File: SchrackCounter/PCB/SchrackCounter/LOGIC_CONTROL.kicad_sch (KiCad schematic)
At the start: 7 parts, among them U1 LTD080BUE-103A, U2 LTD080BUE-103A, U3 LTD080BUE-103A, U6 MAX7219

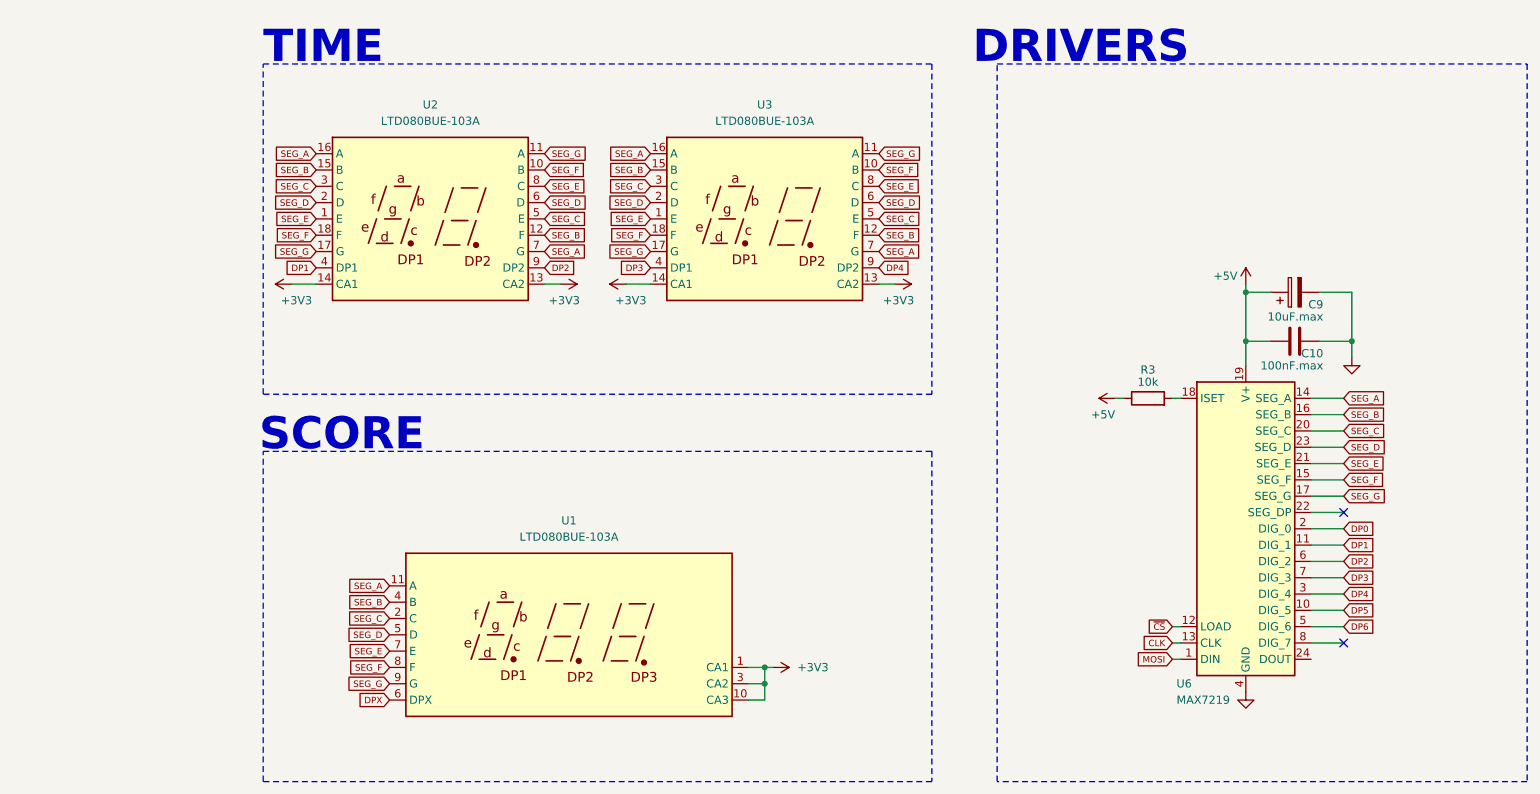
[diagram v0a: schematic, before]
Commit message: SD card addition
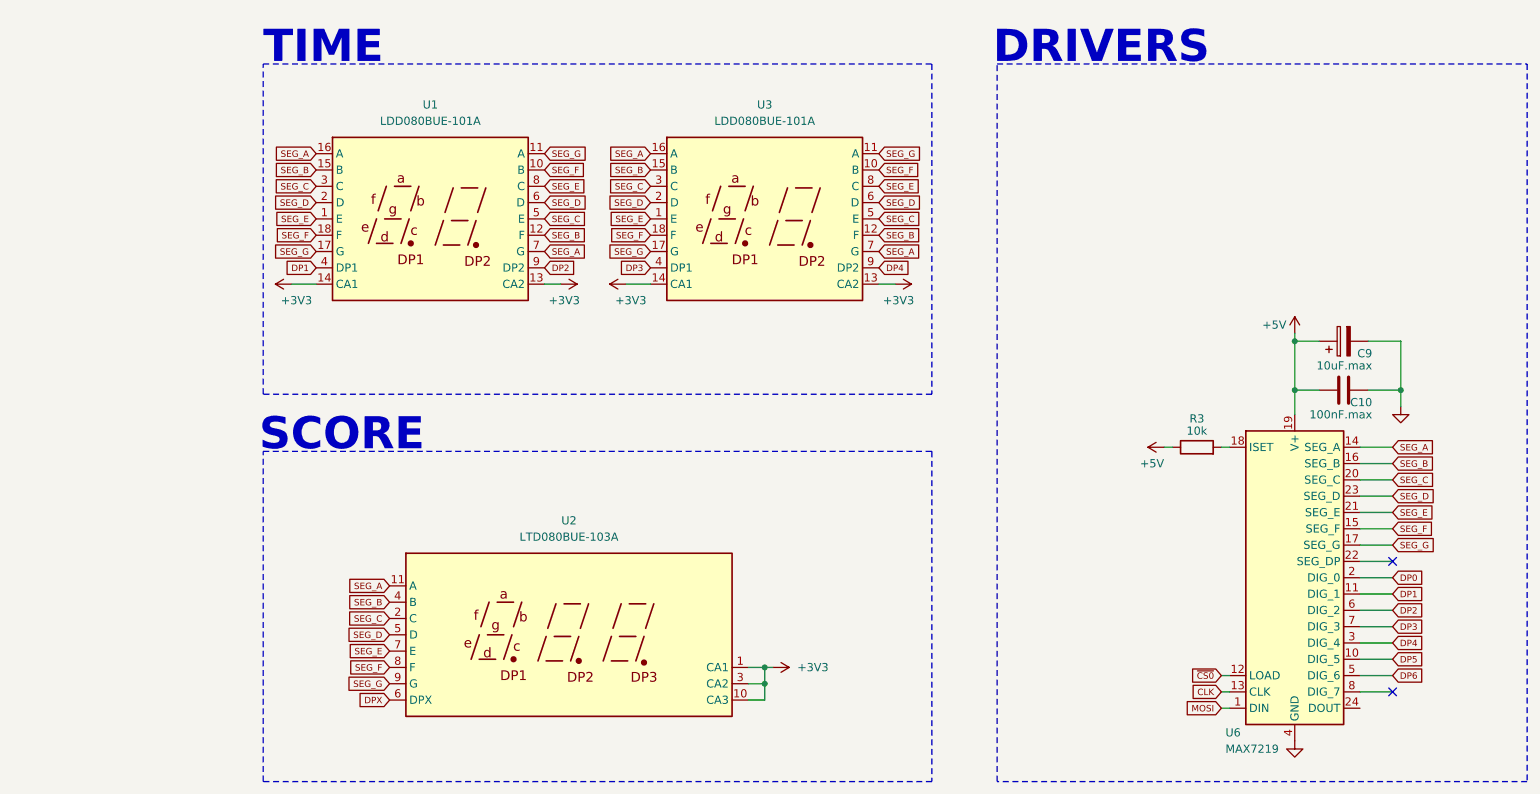
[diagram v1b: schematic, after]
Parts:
- removed U1: LTD080BUE-103A, Schrack_brd:LTD080BUE-103A_made_by_bismarx, symbol sumec_sch_lib:LTD080BUE-103A_made_by_bismarx
- removed U2, U3: LTD080BUE-103A, Schrack_brd:LDD080BUE-101A_made_by_bismarx, symbol sumec_sch_lib:LTD080BUE-103A_made_by_bismarx
- added U1, U3: LDD080BUE-101A, Schrack_brd:LDD080BUE-101A_made_by_bismarx, symbol SchrackThingy_library:LDD080BUE-101A_made_by_bismarx
- added U2: LTD080BUE-103A, Schrack_brd:LTD080BUE-103A_made_by_bismarx, symbol SchrackThingy_library:LTD080BUE-103A_made_by_bismarx
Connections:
- net +3V3: now also U1.13 (CA2), U1.14 (CA1), U2.1 (CA1), U2.10 (CA3), U2.3 (CA2), U3.13 (CA2), U3.14 (CA1)
- net DP1: now also U1.4 (DP1)
- net DP2: now also U1.9 (DP2)
- net DP3: now also U3.4 (DP1)
- net DP4: now also U3.9 (DP2)
- net DPX: now also U2.6 (DPX)
- net SEG_A: now also U1.16 (A), U1.7 (G), U2.11 (A), U3.16 (A), U3.7 (G)
- net SEG_B: now also U1.12 (F), U1.15 (B), U2.4 (B), U3.12 (F), U3.15 (B)
- net SEG_C: now also U1.3 (C), U1.5 (E), U2.2 (C), U3.3 (C), U3.5 (E)
- net SEG_D: now also U1.2 (D), U1.6 (D), U2.5 (D), U3.2 (D), U3.6 (D)
- net SEG_E: now also U1.1 (E), U1.8 (C), U2.7 (E), U3.1 (E), U3.8 (C)
- net SEG_F: now also U1.10 (B), U1.18 (F), U2.8 (F), U3.10 (B), U3.18 (F)
- net SEG_G: now also U1.11 (A), U1.17 (G), U2.9 (G), U3.11 (A), U3.17 (G)
- net ~{CS} renamed ~{CS0}
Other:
- moved on the sheet: C10, C9, R3, U6

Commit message: PCB update
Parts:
- renumbered U6 to U4
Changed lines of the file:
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@@
 		(dnp no)
 		(fields_autoplaced yes)
-		(property "Reference" "#PWR022"
+		(property "Reference" "#PWR020"
 			(at 223.52 93.98 0)
 			(effects
@@
 			(project "SchrackCounter"
 				(path "/d96f2ffc-3f4c-4f71-b693-29f6b8c3245d/50491303-1200-42ed-9e6c-90c20c198c18"
-					(reference "#PWR022")
+					(reference "#PWR020")
 					(unit 1)
 				)
@@
 		(on_board yes)
 		(dnp no)
-		(property "Reference" "#PWR015"
+		(property "Reference" "#PWR016"
 			(at 140.97 68.58 0)
 			(effects
@@
 			(project "SchrackCounter"
 				(path "/d96f2ffc-3f4c-4f71-b693-29f6b8c3245d/50491303-1200-42ed-9e6c-90c20c198c18"
-					(reference "#PWR015")
+					(reference "#PWR016")
 					(unit 1)
 				)
@@
 		(on_board yes)
 		(dnp no)
-		(property "Reference" "#PWR020"
+		(property "Reference" "#PWR018"
 			(at 207.01 80.01 0)
 			(effects
@@
 			(project "SchrackCounter"
 				(path "/d96f2ffc-3f4c-4f71-b693-29f6b8c3245d/50491303-1200-42ed-9e6c-90c20c198c18"
-					(reference "#PWR020")
+					(reference "#PWR018")
 					(unit 1)
 				)
@@
 		(on_board yes)
 		(dnp no)
-		(property "Reference" "#PWR016"
+		(property "Reference" "#PWR013"
 			(at 88.9 68.58 0)
 			(effects
@@
 			(project "SchrackCounter"
 				(path "/d96f2ffc-3f4c-4f71-b693-29f6b8c3245d/50491303-1200-42ed-9e6c-90c20c198c18"
-					(reference "#PWR016")
+					(reference "#PWR013")
 					(unit 1)
 				)
@@
 		(on_board yes)
 		(dnp no)
-		(property "Reference" "U6"
+		(property "Reference" "U4"
 			(at 196.215 138.43 0)
 			(effects
@@
 			(project ""
 				(path "/d96f2ffc-3f4c-4f71-b693-29f6b8c3245d/50491303-1200-42ed-9e6c-90c20c198c18"
-					(reference "U6")
+					(reference "U4")
 					(unit 1)
 				)
@@
 		(on_board yes)
 		(dnp no)
-		(property "Reference" "#PWR019"
+		(property "Reference" "#PWR017"
 			(at 190.5 93.98 0)
 			(effects
@@
 			(project "SchrackCounter"
 				(path "/d96f2ffc-3f4c-4f71-b693-29f6b8c3245d/50491303-1200-42ed-9e6c-90c20c198c18"
-					(reference "#PWR019")
+					(reference "#PWR017")
 					(unit 1)
 				)
@@
 		(on_board yes)
 		(dnp no)
-		(property "Reference" "#PWR013"
+		(property "Reference" "#PWR015"
 			(at 121.92 128.27 0)
 			(effects
@@
 			(project "SchrackCounter"
 				(path "/d96f2ffc-3f4c-4f71-b693-29f6b8c3245d/50491303-1200-42ed-9e6c-90c20c198c18"
-					(reference "#PWR013")
+					(reference "#PWR015")
 					(unit 1)
 				)
@@
 		(dnp no)
 		(fields_autoplaced yes)
-		(property "Reference" "#PWR021"
+		(property "Reference" "#PWR019"
 			(at 207.01 146.05 0)
 			(effects
@@
 			(project "SchrackCounter"
 				(path "/d96f2ffc-3f4c-4f71-b693-29f6b8c3245d/50491303-1200-42ed-9e6c-90c20c198c18"
-					(reference "#PWR021")
-					(unit 1)
-				)
+					(reference "#PWR019")
+					(unit 1)
+				)

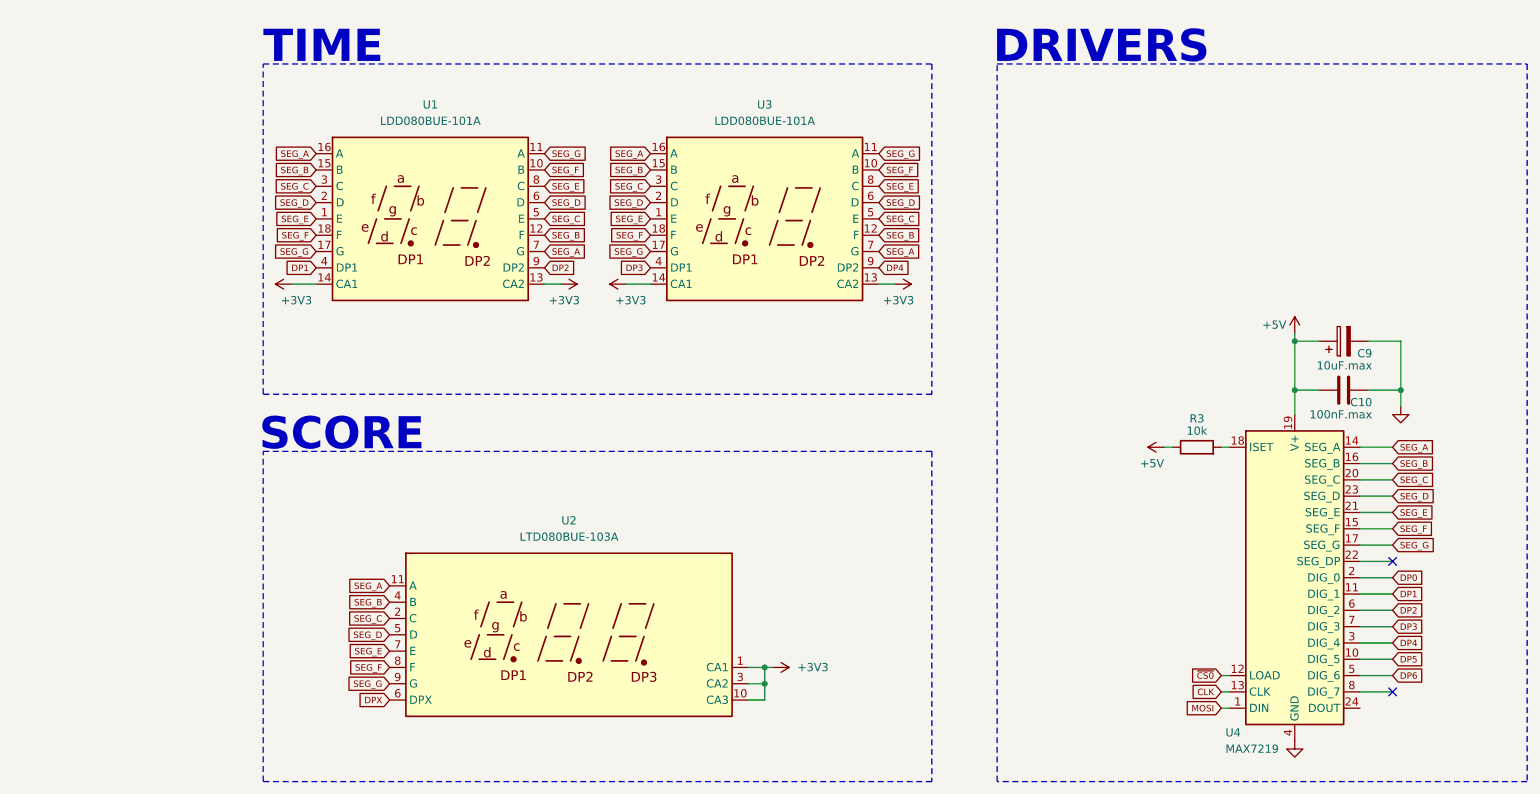
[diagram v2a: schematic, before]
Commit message: Schematic and PCB update
LDO Regulator, and some layout update
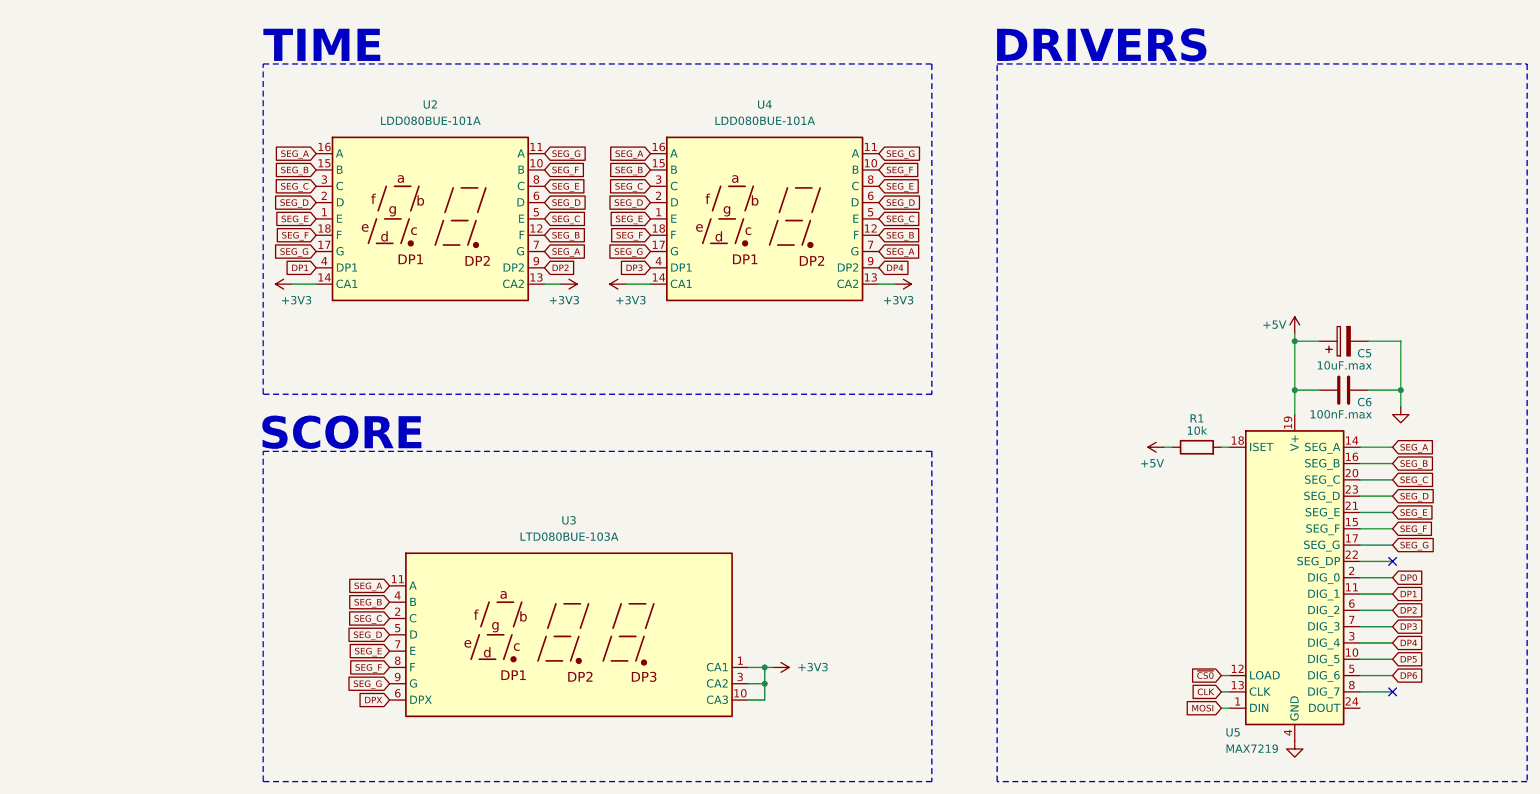
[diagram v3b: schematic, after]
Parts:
- renumbered C9 to C5, C10 to C6, R3 to R1, U1 to U2, U2 to U3, U3 to U4, U4 to U5
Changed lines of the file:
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@@
 		(dnp no)
 		(fields_autoplaced yes)
-		(property "Reference" "#PWR020"
+		(property "Reference" "#PWR014"
 			(at 223.52 93.98 0)
 			(effects
@@
 			(project "SchrackCounter"
 				(path "/d96f2ffc-3f4c-4f71-b693-29f6b8c3245d/50491303-1200-42ed-9e6c-90c20c198c18"
-					(reference "#PWR020")
+					(reference "#PWR014")
 					(unit 1)
 				)
@@
 		(dnp no)
 		(fields_autoplaced yes)
-		(property "Reference" "U1"
+		(property "Reference" "U2"
 			(at 72.39 40.64 0)
 			(effects
@@
 			(project ""
 				(path "/d96f2ffc-3f4c-4f71-b693-29f6b8c3245d/50491303-1200-42ed-9e6c-90c20c198c18"
-					(reference "U1")
+					(reference "U2")
 					(unit 1)
 				)
@@
 		(on_board yes)
 		(dnp no)
-		(property "Reference" "#PWR016"
+		(property "Reference" "#PWR010"
 			(at 140.97 68.58 0)
 			(effects
@@
 			(project "SchrackCounter"
 				(path "/d96f2ffc-3f4c-4f71-b693-29f6b8c3245d/50491303-1200-42ed-9e6c-90c20c198c18"
-					(reference "#PWR016")
+					(reference "#PWR010")
 					(unit 1)
 				)
@@
 		(on_board yes)
 		(dnp no)
-		(property "Reference" "C9"
+		(property "Reference" "C5"
 			(at 219.075 79.375 90)
 			(effects
@@
 			(project "SchrackCounter"
 				(path "/d96f2ffc-3f4c-4f71-b693-29f6b8c3245d/50491303-1200-42ed-9e6c-90c20c198c18"
-					(reference "C9")
+					(reference "C5")
 					(unit 1)
 				)
@@
 		(on_board yes)
 		(dnp no)
-		(property "Reference" "C10"
+		(property "Reference" "C6"
 			(at 219.075 86.995 90)
 			(effects
@@
 			(project "SchrackCounter"
 				(path "/d96f2ffc-3f4c-4f71-b693-29f6b8c3245d/50491303-1200-42ed-9e6c-90c20c198c18"
-					(reference "C10")
+					(reference "C6")
 					(unit 1)
 				)
@@
 		(dnp no)
 		(fields_autoplaced yes)
-		(property "Reference" "U2"
+		(property "Reference" "U3"
 			(at 93.98 105.41 0)
 			(effects
@@
 			(project ""
 				(path "/d96f2ffc-3f4c-4f71-b693-29f6b8c3245d/50491303-1200-42ed-9e6c-90c20c198c18"
-					(reference "U2")
+					(reference "U3")
 					(unit 1)
 				)
@@
 		(on_board yes)
 		(dnp no)
-		(property "Reference" "#PWR018"
+		(property "Reference" "#PWR012"
 			(at 207.01 80.01 0)
 			(effects
@@
 			(project "SchrackCounter"
 				(path "/d96f2ffc-3f4c-4f71-b693-29f6b8c3245d/50491303-1200-42ed-9e6c-90c20c198c18"
-					(reference "#PWR018")
+					(reference "#PWR012")
 					(unit 1)
 				)
@@
 		(on_board yes)
 		(dnp no)
-		(property "Reference" "R3"
+		(property "Reference" "R1"
 			(at 191.77 89.535 90)
 			(effects
@@
 			(project "SchrackCounter"
 				(path "/d96f2ffc-3f4c-4f71-b693-29f6b8c3245d/50491303-1200-42ed-9e6c-90c20c198c18"
-					(reference "R3")
+					(reference "R1")
 					(unit 1)
 				)
@@
 		(on_board yes)
 		(dnp no)
-		(property "Reference" "#PWR013"
+		(property "Reference" "#PWR07"
 			(at 88.9 68.58 0)
 			(effects
@@
 			(project "SchrackCounter"
 				(path "/d96f2ffc-3f4c-4f71-b693-29f6b8c3245d/50491303-1200-42ed-9e6c-90c20c198c18"
-					(reference "#PWR013")
+					(reference "#PWR07")
 					(unit 1)
 				)
@@
 		(on_board yes)
 		(dnp no)
-		(property "Reference" "#PWR012"
+		(property "Reference" "#PWR06"
 			(at 54.61 68.58 0)
 			(effects
@@
 			(project "SchrackCounter"
 				(path "/d96f2ffc-3f4c-4f71-b693-29f6b8c3245d/50491303-1200-42ed-9e6c-90c20c198c18"
-					(reference "#PWR012")
+					(reference "#PWR06")
 					(unit 1)
 				)
@@
 		(on_board yes)
 		(dnp no)
-		(property "Reference" "U4"
+		(property "Reference" "U5"
 			(at 196.215 138.43 0)
 			(effects
@@
 			(project ""
 				(path "/d96f2ffc-3f4c-4f71-b693-29f6b8c3245d/50491303-1200-42ed-9e6c-90c20c198c18"
-					(reference "U4")
+					(reference "U5")
 					(unit 1)
 				)
@@
 		(dnp no)
 		(fields_autoplaced yes)
-		(property "Reference" "U3"
+		(property "Reference" "U4"
 			(at 124.46 40.64 0)
 			(effects
@@
 			(project "SchrackCounter"
 				(path "/d96f2ffc-3f4c-4f71-b693-29f6b8c3245d/50491303-1200-42ed-9e6c-90c20c198c18"
-					(reference "U3")
+					(reference "U4")
 					(unit 1)
 				)
@@
 		(on_board yes)
 		(dnp no)
-		(property "Reference" "#PWR014"
+		(property "Reference" "#PWR08"
 			(at 106.68 68.58 0)
 			(effects
@@
 			(project "SchrackCounter"
 				(path "/d96f2ffc-3f4c-4f71-b693-29f6b8c3245d/50491303-1200-42ed-9e6c-90c20c198c18"
-					(reference "#PWR014")
+					(reference "#PWR08")
 					(unit 1)
 				)
@@
 		(on_board yes)
 		(dnp no)
-		(property "Reference" "#PWR017"
+		(property "Reference" "#PWR011"
 			(at 190.5 93.98 0)
 			(effects
@@
 			(project "SchrackCounter"
 				(path "/d96f2ffc-3f4c-4f71-b693-29f6b8c3245d/50491303-1200-42ed-9e6c-90c20c198c18"
-					(reference "#PWR017")
+					(reference "#PWR011")
 					(unit 1)
 				)
@@
 		(on_board yes)
 		(dnp no)
-		(property "Reference" "#PWR015"
+		(property "Reference" "#PWR09"
 			(at 121.92 128.27 0)
 			(effects
@@
 			(project "SchrackCounter"
 				(path "/d96f2ffc-3f4c-4f71-b693-29f6b8c3245d/50491303-1200-42ed-9e6c-90c20c198c18"
-					(reference "#PWR015")
+					(reference "#PWR09")
 					(unit 1)
 				)
@@
 		(dnp no)
 		(fields_autoplaced yes)
-		(property "Reference" "#PWR019"
+		(property "Reference" "#PWR013"
 			(at 207.01 146.05 0)
 			(effects
@@
 			(project "SchrackCounter"
 				(path "/d96f2ffc-3f4c-4f71-b693-29f6b8c3245d/50491303-1200-42ed-9e6c-90c20c198c18"
-					(reference "#PWR019")
-					(unit 1)
-				)
+					(reference "#PWR013")
+					(unit 1)
+				)

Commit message: PCB layout update
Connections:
- no-connect marks 2 -> 3
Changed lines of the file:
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@@
+	)
+	(no_connect
+		(at 222.25 134.62)
 	)
 	(no_connect
@@
 		(pts
 			(xy 222.25 101.6) (xy 217.17 101.6)
+		)
+		(stroke
+			(width 0)
+			(type default)
+		)
+	)
+	(wire
+		(pts
+			(xy 217.17 134.62) (xy 222.25 134.62)
 		)
 		(stroke
@@
 		(on_board yes)
 		(dnp no)
-		(fields_autoplaced yes)
 		(property "Reference" "U2"
-			(at 72.39 40.64 0)
+			(at 72.39 41.275 0)
 			(effects
 				(font
@@
 		)
 		(property "Value" "LDD080BUE-101A"
-			(at 72.39 43.18 0)
+			(at 72.39 43.815 0)
 			(effects
 				(font
@@
 		(on_board yes)
 		(dnp no)
-		(fields_autoplaced yes)
 		(property "Reference" "U3"
-			(at 93.98 105.41 0)
+			(at 93.98 106.045 0)
 			(effects
 				(font
@@
 		)
 		(property "Value" "LTD080BUE-103A"
-			(at 93.98 107.95 0)
+			(at 93.98 108.585 0)
 			(effects
 				(font
@@
 		(dnp no)
 		(property "Reference" "U5"
-			(at 196.215 138.43 0)
+			(at 196.215 139.065 0)
 			(effects
 				(font
@@
 		(on_board yes)
 		(dnp no)
-		(fields_autoplaced yes)
 		(property "Reference" "U4"
-			(at 124.46 40.64 0)
+			(at 124.46 41.275 0)
 			(effects
 				(font
@@
 		)
 		(property "Value" "LDD080BUE-101A"
-			(at 124.46 43.18 0)
-			(effects
-				(font
+			(at 124.46 43.815 0)
+			(effects
+				(font

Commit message: Schrack pcb updates
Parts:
- U5: footprint Package_SO:SOIC-24W_7.5x15.4mm_P1.27mm -> Package_DIP:DIP-24_W10.16mm
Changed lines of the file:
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@@
 			)
 		)
-		(property "Footprint" "Package_SO:SOIC-24W_7.5x15.4mm_P1.27mm"
+		(property "Footprint" "Package_DIP:DIP-24_W10.16mm"
 			(at 205.74 113.03 0)
 			(effects
